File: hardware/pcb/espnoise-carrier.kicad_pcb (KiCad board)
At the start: 2 copper layers, 96 x 38 mm, 17 parts, among them J1 5V INPUT, J2 CONTROLLER, J3 LED STRIP, J4 MICROPHONE, J5 BUZZER, Q1 MMBT3904, SW1 MUTE, SW2 BUZZER ENABLE, U1 SN74AHCT125PWR

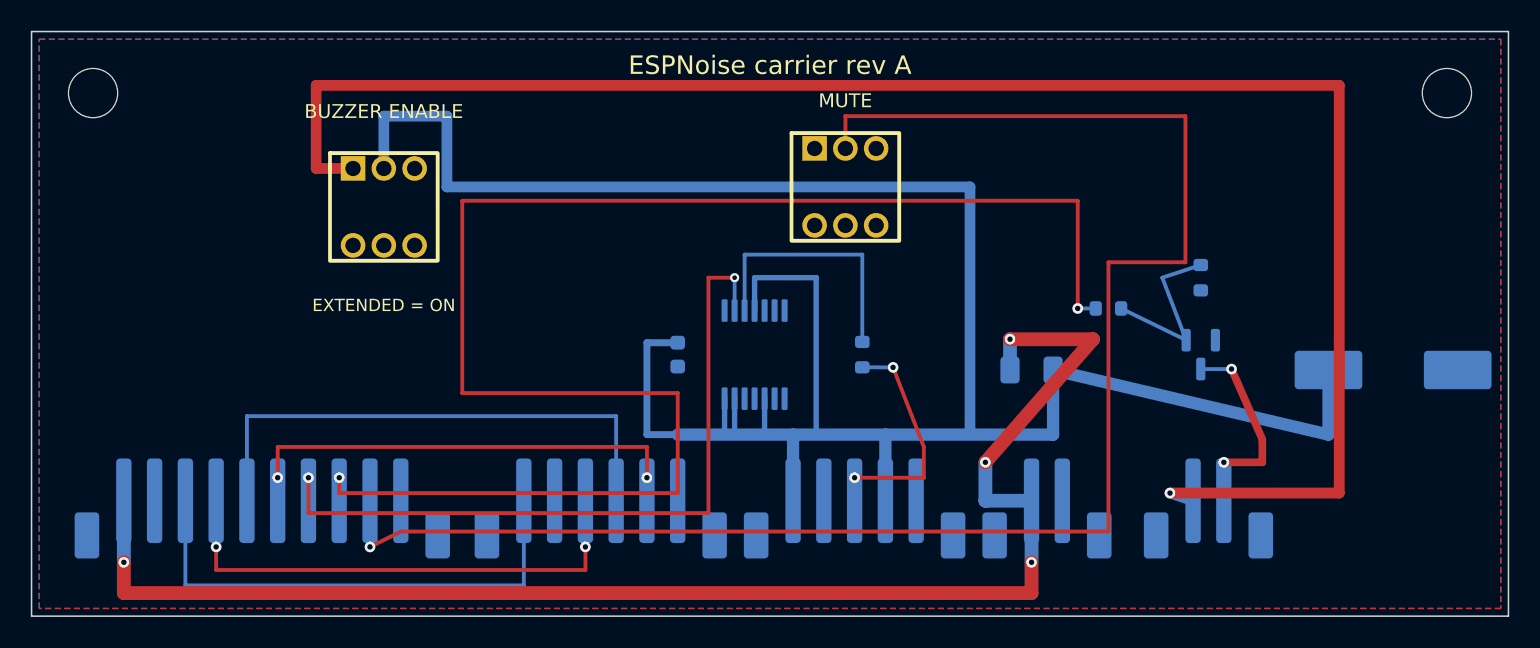
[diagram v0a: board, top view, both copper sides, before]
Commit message: Redesign carrier PCB for the 80 mm case
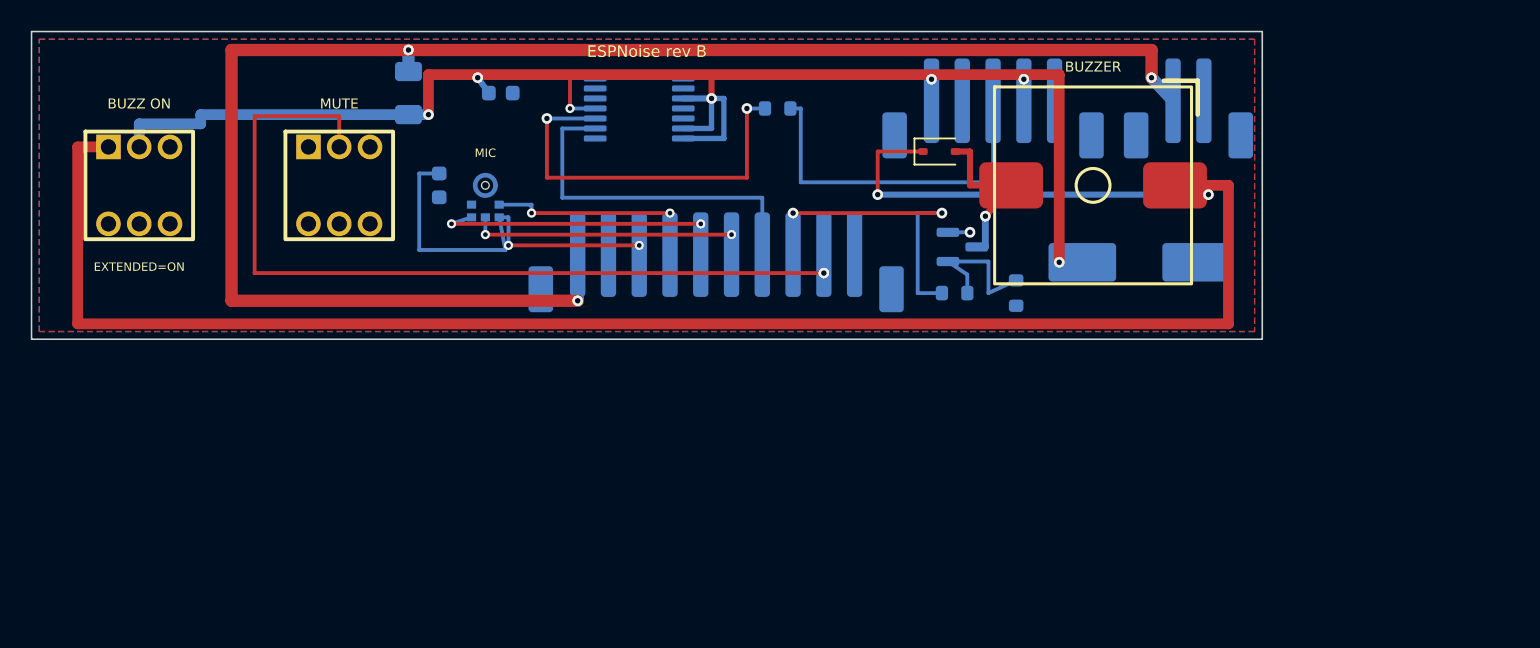
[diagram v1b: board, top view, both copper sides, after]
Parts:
- removed H1, H2: M3 mounting hole, MountingHole_3.2mm_M3
- removed J4: MICROPHONE, JST_PH_B6B-PH-SM4-TB_1x06-1MP_P2.00mm_Vertical
- removed J5: BUZZER, JST_PH_B2B-PH-SM4-TB_1x02-1MP_P2.00mm_Vertical
- added BZ1: FUET-1370F-05, ESPNoise_FUET-1370F-05, F.Cu at (69.0, 10.0)
- added C3: 100nF, C_0603_1608Metric, B.Cu at (26.5, 10.0)
- added D1: 1N5819WS, D_SOD-323, F.Cu at (59.0, 7.80)
- added MIC1: ICS-43434, InvenSense_ICS-43434-6_3.5x2.65mm, B.Cu at (29.5, 10.7)
- C2: value 1000uF 16V -> 1000uF 10V; footprint CP_Elec_10x10.5 -> CP_Elec_8x10.5
- J1: value 5V INPUT -> USB-C 5V
- R2: value 5.1k -> 1k
- moved F1 44.3 mm to (24.5, 4.00), turned to -90 degrees
- moved J2 33.6 mm to (44.5, 15.0)
- moved SW1 32.9 mm to (20.0, 10.0)
- moved J1 27.6 mm to (75.2, 5.00)
- moved J3 27.5 mm to (62.5, 5.00)
- moved C1 20.5 mm to (30.5, 4.00), turned to 0 degrees
- moved C2 17.9 mm to (72.0, 15.0)
- moved U1 17.7 mm to (39.5, 5.00), turned to 0 degrees
- moved Q1 17.0 mm to (60.5, 14.0), turned to 0 degrees
- moved R1 16.9 mm to (48.5, 5.00), turned to 0 degrees
- moved SW2 16.0 mm to (7.00, 10.0)
- moved R3 12.0 mm to (64.0, 17.0)
- moved R2 10.0 mm to (60.0, 17.0)
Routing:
- net BUZZER_PWM: track 105.7 -> 20.7 mm
- net +5V_PERIPH: track 155.3 -> 100.1 mm, vias 0 -> 7
- net MUTE_N: track 107.4 -> 55.9 mm
- net LED_DATA_3V3: track 48.9 -> 23.3 mm, vias 2 -> 0
- net MIC_SCK: track 33.0 -> 14.3 mm
- net +5V_BUZZER_SW: track 113.4 -> 130.3 mm, vias 1 -> 2
- net MIC_WS: track 35.0 -> 19.6 mm, vias 0 -> 2
- net MIC_SD: track 31.0 -> 18.4 mm
- net +5V_IN: track 94.5 -> 106.9 mm, vias 4 -> 3
- net LED_DATA_5V_RAW: track 17.0 -> 25.7 mm, vias 0 -> 2
- net LED_DATA_5V: track 15.5 -> 23.3 mm, vias 2 -> 0
- net +3V3: track 33.0 -> 25.6 mm, vias 0 -> 2
- net BUZZER_COLLECTOR: track 13.5 -> 11.0 mm, vias 2 -> 1
- net BUZZER_BASE: track 11.7 -> 9.39 mm
- net GND: track 0.00 -> 1.44 mm, vias 0 -> 1
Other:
- board size 96 x 38 mm -> 80 x 20 mm
- board text added: "BOTTOM - CONNECTORS DOWN"
- board text added: "BUZZ ON"
- board text added: "BUZZER"
- board text added: "ESPNoise rev B"
- board text added: "EXTENDED=ON"
- board text added: "J1 USB-C 5V"
- board text added: "J2 CTRL"
- board text added: "J3 LED"
- board text added: "MIC"
- board text removed: "BUZZER ENABLE"
- board text removed: "ESPNoise carrier rev A"
- board text removed: "EXTENDED = ON"
- board text removed: "J2 CTRL J4 MIC J3 LED J1 5V J5 BUZZ"
- board text removed: "LOWER FACE - CABLES DOWN"
